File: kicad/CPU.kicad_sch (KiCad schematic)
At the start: 13 parts, among them U3 68010P10, U4 GAL22V10, U5 SST39SF040, U6 AS6C4008-55PCN, U7 SST39SF040, U8 AS6C4008-55PCN

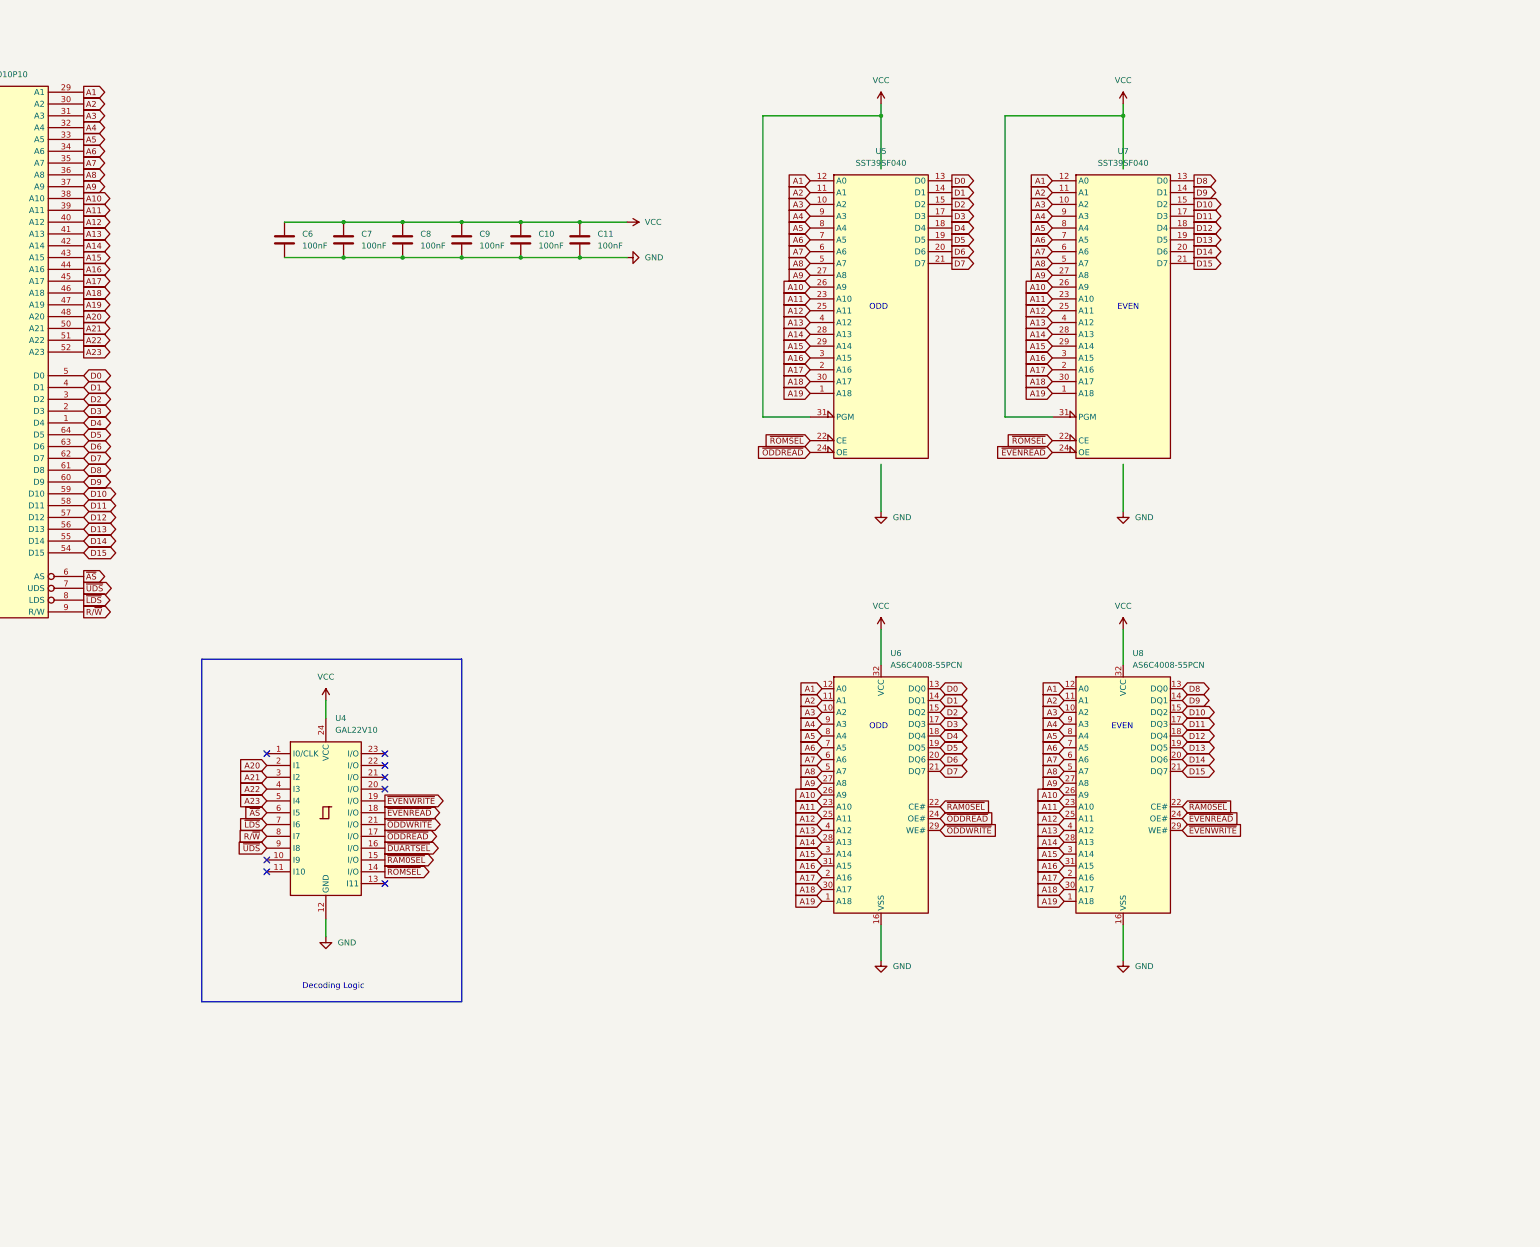
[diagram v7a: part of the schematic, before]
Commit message: New decoding and GALs
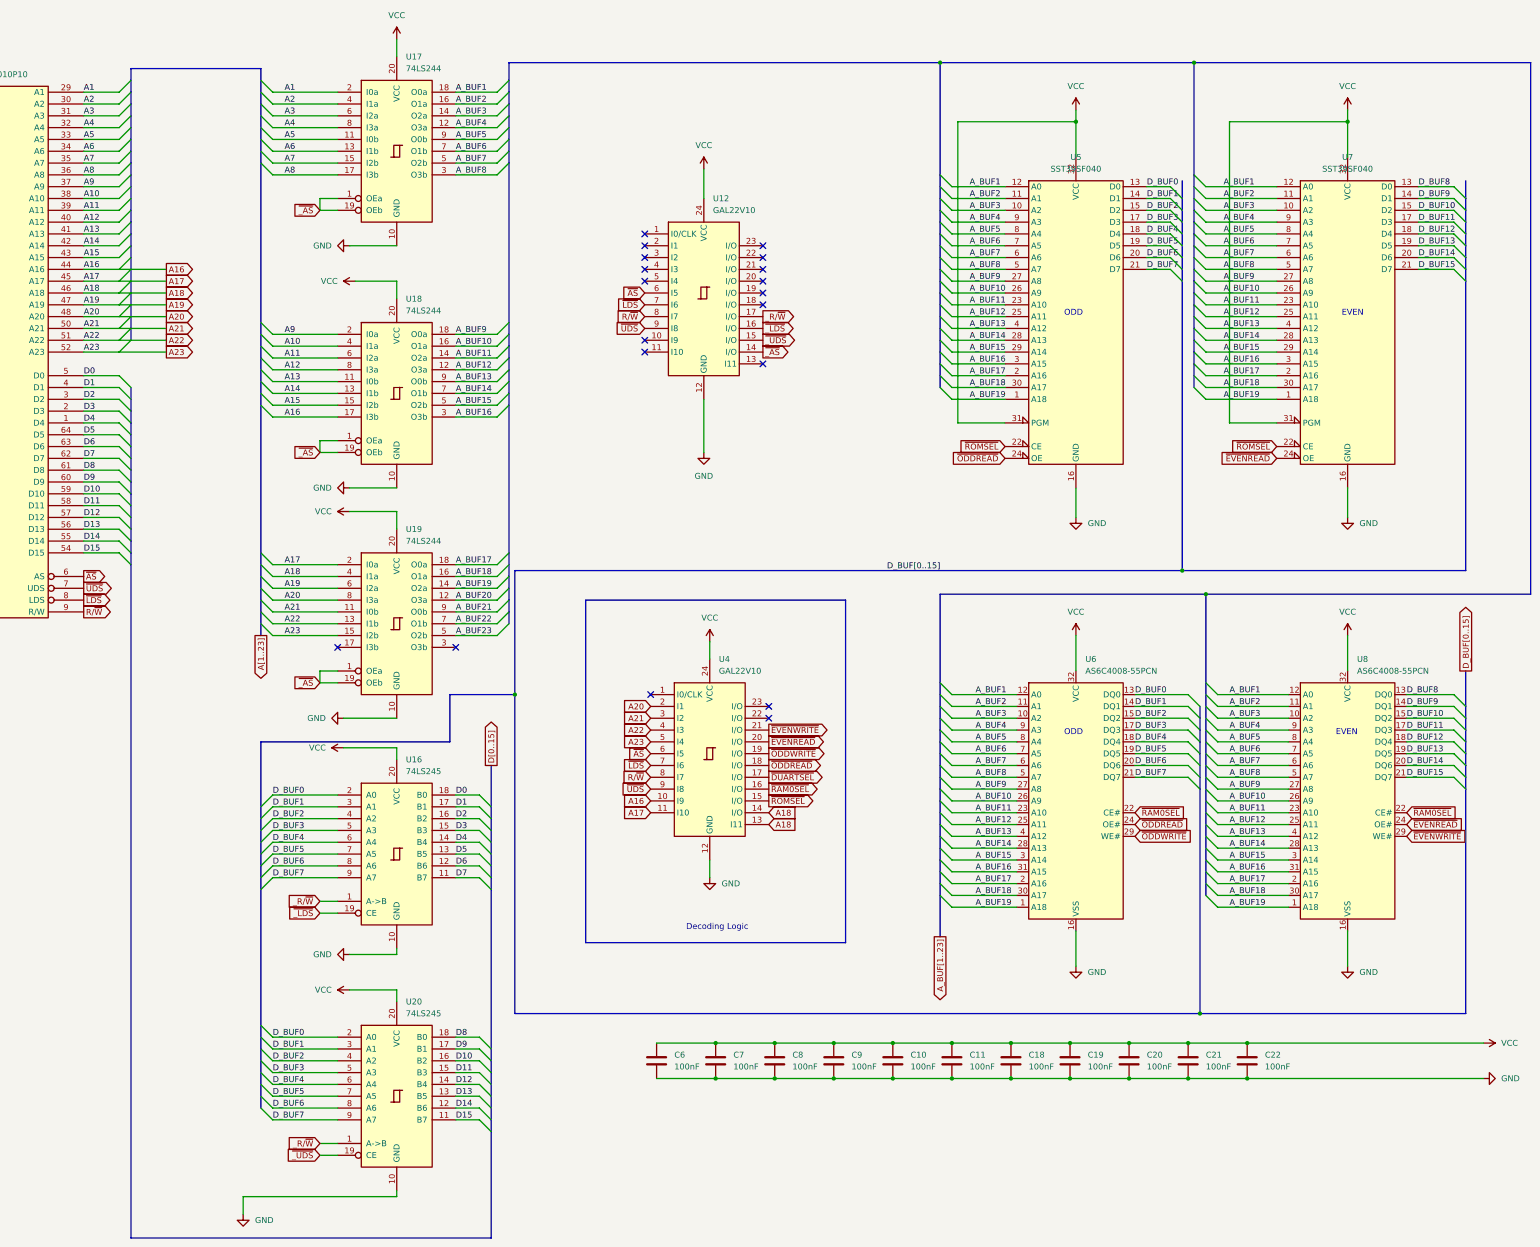
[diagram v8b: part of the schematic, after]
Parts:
- added C18, C19, C20, C21, C22: 100nF, Capacitor_THT:CP_Radial_D5.0mm_P2.50mm, symbol Device:C
- added U12: GAL22V10, symbol Lattice_GAL_sym:GAL22V10
- added U16, U20: 74LS245, symbol 74xx:74LS245
- added U17, U18, U19: 74LS244, symbol 74xx:74LS244
- U4: footprint Package_DIP:DIP-24_W7.62mm_Socket -> (none)
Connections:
- net A1: now also U17.2 (I0a); no longer U5.12 (A0), U6.12 (A0), U7.12 (A0), U8.12 (A0)
- net A10: now also U18.4 (I1a); no longer U5.26 (A9), U6.26 (A9), U7.26 (A9), U8.26 (A9)
- net A11: now also U18.6 (I2a); no longer U5.23 (A10), U6.23 (A10), U7.23 (A10), U8.23 (A10)
- net A12: now also U18.8 (I3a); no longer U5.25 (A11), U6.25 (A11), U7.25 (A11), U8.25 (A11)
- net A13: now also U18.11 (I0b); no longer U5.4 (A12), U6.4 (A12), U7.4 (A12), U8.4 (A12)
- net A14: now also U18.13 (I1b); no longer U5.28 (A13), U6.28 (A13), U7.28 (A13), U8.28 (A13)
- net A15: now also U18.15 (I2b); no longer U5.29 (A14), U6.3 (A14), U7.29 (A14), U8.3 (A14)
- net A16: now also U4.10 (I9), U18.17 (I3b); no longer U5.3 (A15), U6.31 (A15), U7.3 (A15), U8.31 (A15)
- net A17: now also U4.11 (I10), U19.2 (I0a); no longer U5.2 (A16), U6.2 (A16), U7.2 (A16), U8.2 (A16)
- net A18: now also U4.13 (I11), U4.14 (I/O), U19.4 (I1a); no longer U5.30 (A17), U6.30 (A17), U7.30 (A17), U8.30 (A17)
- net A19: now also U19.6 (I2a); no longer U5.1 (A18), U6.1 (A18), U7.1 (A18), U8.1 (A18)
- net A2: now also U17.4 (I1a); no longer U5.11 (A1), U6.11 (A1), U7.11 (A1), U8.11 (A1)
- net A20: now also U19.8 (I3a)
- net A21: now also U19.11 (I0b)
- net A22: now also U19.13 (I1b)
- net A23: now also U19.15 (I2b)
- net A3: now also U17.6 (I2a); no longer U5.10 (A2), U6.10 (A2), U7.10 (A2), U8.10 (A2)
- net A4: now also U17.8 (I3a); no longer U5.9 (A3), U6.9 (A3), U7.9 (A3), U8.9 (A3)
- net A5: now also U17.11 (I0b); no longer U5.8 (A4), U6.8 (A4), U7.8 (A4), U8.8 (A4)
- net A6: now also U17.13 (I1b); no longer U5.7 (A5), U6.7 (A5), U7.7 (A5), U8.7 (A5)
- net A7: now also U17.15 (I2b); no longer U5.6 (A6), U6.6 (A6), U7.6 (A6), U8.6 (A6)
- net A8: now also U17.17 (I3b); no longer U5.5 (A7), U6.5 (A7), U7.5 (A7), U8.5 (A7)
- net A9: now also U18.2 (I0a); no longer U5.27 (A8), U6.27 (A8), U7.27 (A8), U8.27 (A8)
- net D0: now also U16.18 (B0); no longer U5.13 (D0), U6.13 (DQ0)
- net D1: now also U16.17 (B1); no longer U5.14 (D1), U6.14 (DQ1)
- net D10: now also U20.16 (B2); no longer U7.15 (D2), U8.15 (DQ2)
- net D11: now also U20.15 (B3); no longer U7.17 (D3), U8.17 (DQ3)
- net D12: now also U20.14 (B4); no longer U7.18 (D4), U8.18 (DQ4)
- net D13: now also U20.13 (B5); no longer U7.19 (D5), U8.19 (DQ5)
- net D14: now also U20.12 (B6); no longer U7.20 (D6), U8.20 (DQ6)
- net D15: now also U20.11 (B7); no longer U7.21 (D7), U8.21 (DQ7)
- net D2: now also U16.16 (B2); no longer U5.15 (D2), U6.15 (DQ2)
- net D3: now also U16.15 (B3); no longer U5.17 (D3), U6.17 (DQ3)
- net D4: now also U16.14 (B4); no longer U5.18 (D4), U6.18 (DQ4)
- net D5: now also U16.13 (B5); no longer U5.19 (D5), U6.19 (DQ5)
- net D6: now also U16.12 (B6); no longer U5.20 (D6), U6.20 (DQ6)
- net D7: now also U16.11 (B7); no longer U5.21 (D7), U6.21 (DQ7)
- net D8: now also U20.18 (B0); no longer U7.13 (D0), U8.13 (DQ0)
- net D9: now also U20.17 (B1); no longer U7.14 (D1), U8.14 (DQ1)
- net GND: now also C18.2, C19.2, C20.2, C21.2, C22.2, U12.12 (GND), U16.10 (GND), U17.10 (GND), U18.10 (GND), U19.10 (GND), U20.10 (GND)
- net R/~{W}: now also U12.8 (I7)
- net VCC: now also C18.1, C19.1, C20.1, C21.1, C22.1, U12.24 (VCC), U16.20 (VCC), U17.20 (VCC), U18.20 (VCC), U19.20 (VCC), U20.20 (VCC)
- net ~{AS}: now also U12.6 (I5)
- net ~{DUARTSEL}: now also U4.17 (I/O); no longer U4.16 (I/O)
- net ~{EVENREAD}: now also U4.20 (I/O); no longer U4.18 (I/O)
- net ~{EVENWRITE}: now also U4.21 (I/O); no longer U4.19 (I/O)
- net ~{LDS}: now also U12.7 (I6)
- net ~{ODDREAD}: now also U4.18 (I/O); no longer U4.17 (I/O)
- net ~{ODDWRITE}: now also U4.19 (I/O); no longer U4.21 (I/O)
- net ~{RAM0SEL}: now also U4.16 (I/O); no longer U4.15 (I/O)
- net ~{ROMSEL}: now also U4.15 (I/O); no longer U4.14 (I/O)
- net ~{UDS}: now also U12.9 (I8)
- new net A_BUF1: U17.18 (O0a), U5.12 (A0), U6.12 (A0), U7.12 (A0), U8.12 (A0)
- new net A_BUF10: U18.16 (O1a), U5.26 (A9), U6.26 (A9), U7.26 (A9), U8.26 (A9)
- new net A_BUF11: U18.14 (O2a), U5.23 (A10), U6.23 (A10), U7.23 (A10), U8.23 (A10)
- new net A_BUF12: U18.12 (O3a), U5.25 (A11), U6.25 (A11), U7.25 (A11), U8.25 (A11)
- new net A_BUF13: U18.9 (O0b), U5.4 (A12), U6.4 (A12), U7.4 (A12), U8.4 (A12)
- new net A_BUF14: U18.7 (O1b), U5.28 (A13), U6.28 (A13), U7.28 (A13), U8.28 (A13)
- new net A_BUF15: U18.5 (O2b), U5.29 (A14), U6.3 (A14), U7.29 (A14), U8.3 (A14)
- new net A_BUF16: U18.3 (O3b), U5.3 (A15), U6.31 (A15), U7.3 (A15), U8.31 (A15)
- new net A_BUF17: U19.18 (O0a), U5.2 (A16), U6.2 (A16), U7.2 (A16), U8.2 (A16)
- new net A_BUF18: U19.16 (O1a), U5.30 (A17), U6.30 (A17), U7.30 (A17), U8.30 (A17)
- new net A_BUF19: U19.14 (O2a), U5.1 (A18), U6.1 (A18), U7.1 (A18), U8.1 (A18)
- new net A_BUF2: U17.16 (O1a), U5.11 (A1), U6.11 (A1), U7.11 (A1), U8.11 (A1)
- new net A_BUF20: U19.12 (O3a)
- new net A_BUF21: U19.9 (O0b)
- new net A_BUF22: U19.7 (O1b)
- new net A_BUF23: U19.5 (O2b)
- new net A_BUF3: U17.14 (O2a), U5.10 (A2), U6.10 (A2), U7.10 (A2), U8.10 (A2)
- new net A_BUF4: U17.12 (O3a), U5.9 (A3), U6.9 (A3), U7.9 (A3), U8.9 (A3)
- new net A_BUF5: U17.9 (O0b), U5.8 (A4), U6.8 (A4), U7.8 (A4), U8.8 (A4)
- new net A_BUF6: U17.7 (O1b), U5.7 (A5), U6.7 (A5), U7.7 (A5), U8.7 (A5)
- new net A_BUF7: U17.5 (O2b), U5.6 (A6), U6.6 (A6), U7.6 (A6), U8.6 (A6)
- new net A_BUF8: U17.3 (O3b), U5.5 (A7), U6.5 (A7), U7.5 (A7), U8.5 (A7)
- new net A_BUF9: U18.18 (O0a), U5.27 (A8), U6.27 (A8), U7.27 (A8), U8.27 (A8)
- new net D_BUF0: U16.2 (A0), U20.2 (A0), U5.13 (D0), U6.13 (DQ0)
- new net D_BUF1: U16.3 (A1), U20.3 (A1), U5.14 (D1), U6.14 (DQ1)
- new net D_BUF10: U7.15 (D2), U8.15 (DQ2)
- new net D_BUF11: U7.17 (D3), U8.17 (DQ3)
- new net D_BUF12: U7.18 (D4), U8.18 (DQ4)
- new net D_BUF13: U7.19 (D5), U8.19 (DQ5)
- new net D_BUF14: U7.20 (D6), U8.20 (DQ6)
- new net D_BUF15: U7.21 (D7), U8.21 (DQ7)
- new net D_BUF2: U16.4 (A2), U20.4 (A2), U5.15 (D2), U6.15 (DQ2)
- new net D_BUF3: U16.5 (A3), U20.5 (A3), U5.17 (D3), U6.17 (DQ3)
- new net D_BUF4: U16.6 (A4), U20.6 (A4), U5.18 (D4), U6.18 (DQ4)
- new net D_BUF5: U16.7 (A5), U20.7 (A5), U5.19 (D5), U6.19 (DQ5)
- new net D_BUF6: U16.8 (A6), U20.8 (A6), U5.20 (D6), U6.20 (DQ6)
- new net D_BUF7: U16.9 (A7), U20.9 (A7), U5.21 (D7), U6.21 (DQ7)
- new net D_BUF8: U7.13 (D0), U8.13 (DQ0)
- new net D_BUF9: U7.14 (D1), U8.14 (DQ1)
- new net _R/~{W}: U12.17 (I/O), U16.1 (A->B), U20.1 (A->B)
- new net ~{_AS}: U12.14 (I/O), U17.1 (OEa), U17.19 (OEb), U18.1 (OEa), U18.19 (OEb), U19.1 (OEa), U19.19 (OEb)
- new net ~{_LDS}: U12.16 (I/O), U16.19 (CE)
- new net ~{_UDS}: U12.15 (I/O), U20.19 (CE)
- no-connect marks 11 -> 22
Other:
- moved on the sheet: C10, C11, C6, C7, C8, C9, U6, U8
